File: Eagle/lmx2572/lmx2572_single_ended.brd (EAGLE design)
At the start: 38.1 x 36.9 mm, 36 parts

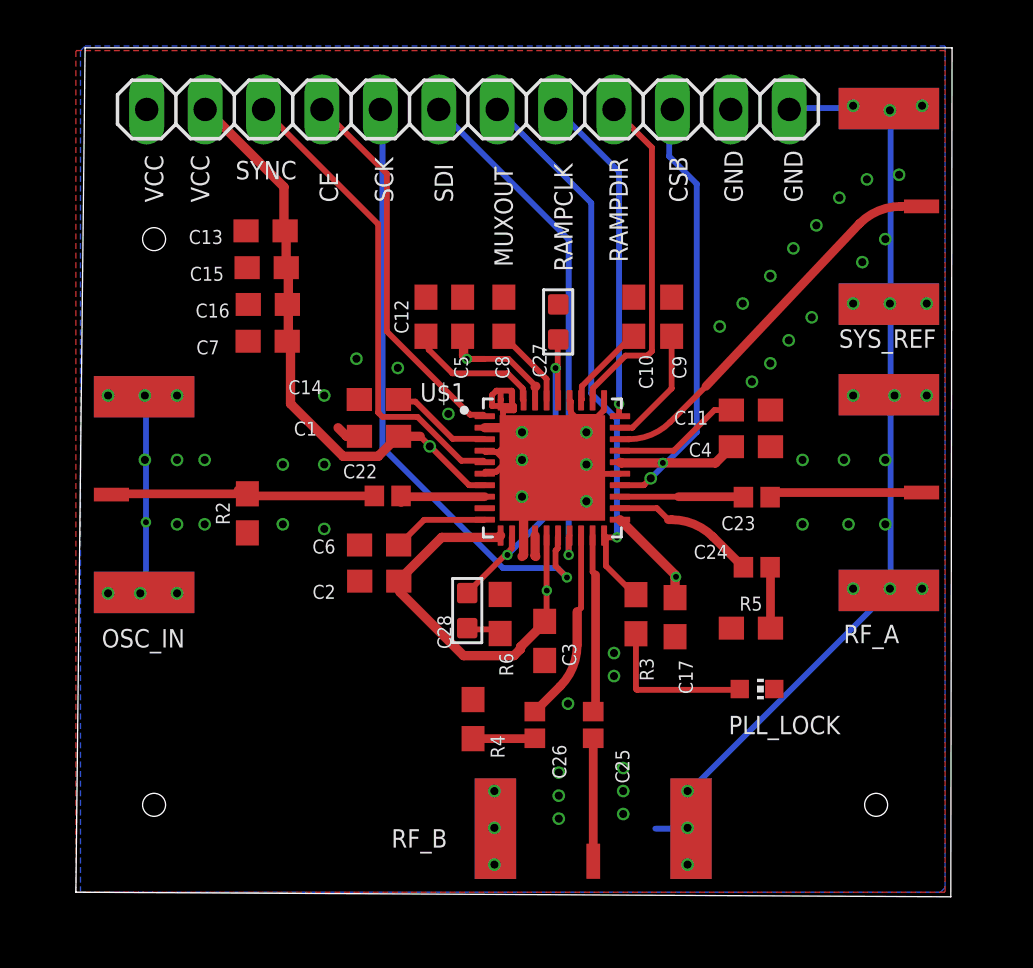
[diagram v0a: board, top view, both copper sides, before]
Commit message: added TCXO
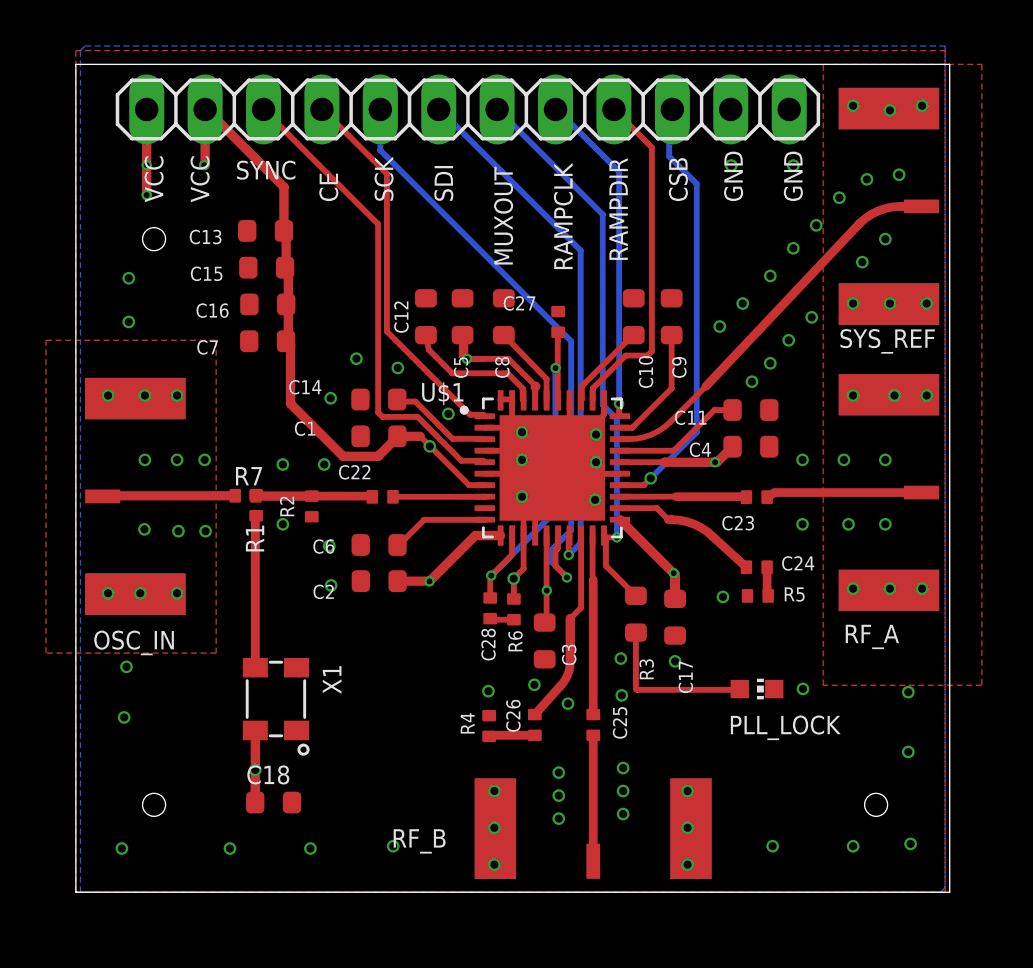
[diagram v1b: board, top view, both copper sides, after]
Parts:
- added C18: 10uF, oresat-rcl:.0603-B-NOSILK
- added R1, R7: 0, oresat-rcl:.0402-C-NOSILK
- added X1: ECS-TXO-3225, X-ECS-TXO-TCXO:3.2X2.5
- C1, C10, C11, C12, C13, C14, C15, C16, C17, C2, C3, C4, C5, C6, C7, C8, C9: device SparkFun-Capacitors:0603 -> oresat-rcl:.0603-B-NOSILK
- C22, C23, C24, C25, C26: device SparkFun-Capacitors:0402 -> oresat-rcl:.0402-C-NOSILK
- C27, C28: device OPL_Capacitor:C0603 -> oresat-rcl:.0402-C-NOSILK
- R2, R4, R5, R6: device SparkFun-Resistors:0603 -> oresat-rcl:.0402-C-NOSILK
- R3: device SparkFun-Resistors:0603 -> oresat-rcl:.0603-B-NOSILK
- moved R2 2.82 mm to (10.3, 16.8)
- moved R5 1.43 mm to (29.7, 12.9)
- moved C28 1.00 mm to (18.0, 12.3), turned to 90 degrees
- moved R4 0.76 mm to (18.0, 7.23)
- moved R6 0.63 mm to (19.1, 12.3)
- moved OSC_IN 0.39 mm to (0.02, 17.2)
- moved C22 0.22 mm to (13.3, 17.2)
- turned C27 to 270 degrees
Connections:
- new net N$11: OSC_IN.RF1, R7.2
- new net N$21: C22.1, R1.2, R2.2, R7.1
- net GND: now also C18.2, X1.2
- net N$9: now also R1.1, X1.3; no longer C22.1, OSC_IN.RF1, R2.2
- net VCC: now also C18.1, X1.4
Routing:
- net GND: track 75.9 -> 33.2 mm, vias 73 -> 95
- net N$11: track 0.00 -> 5.78 mm
- net N$9: track 12.1 -> 6.62 mm
- net N$21: track 0.00 -> 5.08 mm
- net VCC: track 58.2 -> 60.9 mm, vias 5 -> 10
- net N$23: track 2.70 -> 1.27 mm
- net N$24: track 15.1 -> 16.3 mm
- net N$22: track 2.73 -> 2.01 mm
- net SCK: track 27.2 -> 26.6 mm
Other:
- board size 38.1 x 36.9 mm -> 38 x 36 mm

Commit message: more vias
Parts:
- moved RF_A 0.20 mm to (38.0, 17.2)
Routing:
- net GND: track 33.2 -> 34.0 mm, vias 95 -> 97
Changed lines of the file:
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@@
 <drawing>
 <settings>
-<setting alwaysvectorfont="no"/>
+<setting alwaysvectorfont="yes"/>
 <setting verticaltext="up"/>
 </settings>
@@
 <layer number="14" name="Route14" color="22" fill="1" visible="no" active="no"/>
 <layer number="15" name="Route15" color="23" fill="1" visible="no" active="yes"/>
-<layer number="16" name="Bottom" color="1" fill="1" visible="no" active="yes"/>
+<layer number="16" name="Bottom" color="1" fill="1" visible="yes" active="yes"/>
 <layer number="17" name="Pads" color="2" fill="1" visible="yes" active="yes"/>
 <layer number="18" name="Vias" color="2" fill="1" visible="yes" active="yes"/>
@@
 <wire x1="22.6" y1="13.8" x2="22.6" y2="8.4" width="1.27" layer="29"/>
 <wire x1="22.6" y1="6.2" x2="22.6" y2="1" width="1.27" layer="29"/>
-<wire x1="30.6" y1="17.4" x2="37.4" y2="17.4" width="1.27" layer="29"/>
+<wire x1="30.7" y1="17.2" x2="37.5" y2="17.2" width="1.27" layer="29"/>
 <wire x1="27.4" y1="22.2" x2="35" y2="29.8" width="1.27" layer="29"/>
 <wire x1="35" y1="29.8" x2="37.2" y2="29.8" width="1.27" layer="29"/>
@@
 <attribute name="NAME" x="26.546" y="22.826" size="0.6096" layer="25" font="vector" ratio="20" rot="R90" align="bottom-center"/>
 </element>
-<element name="RF_A" library="J-Cinch-142-0701-851-SMA-end-launch" package="142-0701-851" value="142-0701-851" x="37.922" y="17.38" smashed="yes" rot="R270">
-<attribute name="NAME" x="33.382" y="10.83" size="0.8" layer="25" font="vector"/>
+<element name="RF_A" library="J-Cinch-142-0701-851-SMA-end-launch" package="142-0701-851" value="142-0701-851" x="37.962" y="17.18" smashed="yes" rot="R270">
+<attribute name="NAME" x="33.422" y="10.63" size="0.8" layer="25" font="vector"/>
 </element>
 <element name="RF_B" library="J-Cinch-142-0701-851-SMA-end-launch" package="142-0701-851" value="142-0701-851" x="22.498" y="0.2" smashed="yes" rot="R180">
@@
 </polygon>
 <polygon width="0.38" layer="1">
-<vertex x="0.4" y="36.6"/>
-<vertex x="37.8" y="36.6"/>
-<vertex x="37.8" y="0"/>
-<vertex x="0" y="0"/>
 <vertex x="0" y="36.6"/>
+<vertex x="39.62" y="36.6"/>
+<vertex x="39.62" y="-0.02"/>
+<vertex x="0" y="-0.02"/>
 </polygon>
 <wire x1="18.288" y1="2.76225" x2="18.2435" y2="2.766" width="0.254" layer="16"/>
-<wire x1="35.433" y1="13.1445" x2="35.356" y2="13.1255" width="0.254" layer="16"/>
-<wire x1="35.433" y1="21.62175" x2="35.356" y2="21.6345" width="0.254" layer="16"/>
+<wire x1="35.473" y1="12.9445" x2="35.396" y2="12.9255" width="0.254" layer="16"/>
+<wire x1="35.473" y1="21.42175" x2="35.396" y2="21.4345" width="0.254" layer="16"/>
 <wire x1="35.433" y1="25.527" x2="35.356" y2="25.5715" width="0.254" layer="16"/>
-<wire x1="35.433" y1="21.717" x2="35.356" y2="21.6345" width="0.254" layer="16"/>
+<wire x1="35.473" y1="21.517" x2="35.396" y2="21.4345" width="0.254" layer="16"/>
 <wire x1="26.76525" y1="4.47675" x2="26.76525" y2="2.8575" width="0.254" layer="16"/>
 <wire x1="26.76525" y1="2.8575" x2="26.7525" y2="2.766" width="0.254" layer="16"/>
-<wire x1="35.33775" y1="13.04925" x2="35.356" y2="13.1255" width="0.254" layer="16"/>
+<wire x1="35.37775" y1="12.84925" x2="35.396" y2="12.9255" width="0.254" layer="16"/>
 <wire x1="18.57375" y1="18.57375" x2="18.57375" y2="18.8595" width="0.254" layer="1"/>
 <wire x1="18.97" y1="20.17775" x2="18.8448" y2="20.30295" width="0.254" layer="1"/>
-<wire x1="18.57375" y1="20.574" x2="18.8448" y2="20.30295" width="0.254" layer="1"/>
 <wire x1="35.33775" y1="34.0995" x2="35.356" y2="34.0805" width="0.254" layer="16"/>
 <wire x1="31.0515" y1="34.0995" x2="31.02" y2="34.04" width="0.254" layer="16"/>
@@
 </polygon>
 <wire x1="19.729075" y1="16.670925" x2="19.579075" y2="16.520925" width="0.4064" layer="1"/>
-<via x="31.6" y="18.8" extent="1-16" drill="0.35"/>
-<via x="33.4" y="18.8" extent="1-16" drill="0.35"/>
-<via x="35.2" y="18.8" extent="1-16" drill="0.35"/>
-<via x="33.8" y="21.6" extent="1-16" drill="0.35"/>
-<via x="35.6" y="21.6" extent="1-16" drill="0.35"/>
-<via x="37" y="21.6" extent="1-16" drill="0.35"/>
-<via x="35.2" y="16" extent="1-16" drill="0.35"/>
-<via x="33.6" y="16" extent="1-16" drill="0.35"/>
-<via x="31.6" y="16" extent="1-16" drill="0.35"/>
-<via x="33.8" y="13.2" extent="1-16" drill="0.35"/>
-<via x="35.4" y="13.2" extent="1-16" drill="0.35"/>
-<via x="36.8" y="13.2" extent="1-16" drill="0.35"/>
+<via x="31.52" y="18.82" extent="1-16" drill="0.35"/>
+<via x="33.42" y="18.62" extent="1-16" drill="0.35"/>
+<via x="35.2" y="18.62" extent="1-16" drill="0.35"/>
+<via x="33.78" y="21.42" extent="1-16" drill="0.35"/>
+<via x="35.58" y="21.44" extent="1-16" drill="0.35"/>
+<via x="37" y="21.46" extent="1-16" drill="0.35"/>
+<via x="35.26" y="15.88" extent="1-16" drill="0.35"/>
+<via x="33.58" y="15.8" extent="1-16" drill="0.35"/>
+<via x="31.54" y="15.78" extent="1-16" drill="0.35"/>
+<via x="33.86" y="13" extent="1-16" drill="0.35"/>
+<via x="35.46" y="13" extent="1-16" drill="0.35"/>
+<via x="36.82" y="12.96" extent="1-16" drill="0.35"/>
 <via x="37" y="25.6" extent="1-16" drill="0.35"/>
 <via x="35.4" y="25.6" extent="1-16" drill="0.35"/>
@@
 <via x="22.62" y="18.7" extent="1-16" drill="0.35"/>
 <via x="22.58" y="17.06" extent="1-16" drill="0.35"/>
+<wire x1="18.47" y1="21.39" x2="18.47" y2="20.925175" width="0.254" layer="1"/>
+<wire x1="18.47" y1="20.925175" x2="18.479" y2="20.916175" width="0.254" layer="1"/>
+<wire x1="18.479" y1="20.916175" x2="18.479" y2="20.66875" width="0.254" layer="1"/>
+<wire x1="18.479" y1="20.66875" x2="18.8448" y2="20.30295" width="0.254" layer="1"/>
+<via x="15.1" y="27.2" extent="1-16" drill="0.35"/>
+<via x="16.86" y="27.28" extent="1-16" drill="0.35"/>
+<polygon width="0.254" layer="1" thermals="no">
+<vertex x="16.52" y="5.7"/>
+<vertex x="16.52" y="-1.3"/>
+<vertex x="28.96" y="-1.3"/>
+<vertex x="28.96" y="5.7"/>
+</polygon>
 <wire x1="19" y1="19.3" x2="18.57375" y2="18.8595" width="0" layer="19" extent="1-1"/>
 <wire x1="19.14525" y1="19.90725" x2="19" y2="19.3" width="0" layer="19" extent="1-1"/>
 <wire x1="19.2" y1="18.2" x2="19.4" y2="18.8" width="0" layer="19" extent="1-1"/>
-<wire x1="22.97" y1="21.39" x2="22.62" y2="19.9" width="0" layer="19" extent="1-1"/>
 </signal>
 <signal name="N$1">
@@
 <contactref element="C23" pad="2"/>
 <contactref element="RF_A" pad="RF1"/>
-<wire x1="30.06" y1="17.18" x2="30.39" y2="17.38" width="0.381" layer="1"/>
-<wire x1="30.39" y1="17.38" x2="36.776" y2="17.38" width="0.38" layer="1"/>
+<wire x1="36.816" y1="17.18" x2="30.06" y2="17.18" width="0.38" layer="1"/>
 </signal>
 <signal name="N$18" class="2">
@@
 <wire x1="20.955" y1="24.003" x2="20.974" y2="24.35" width="0.254" layer="1"/>
 <wire x1="20.955" y1="21.43125" x2="20.97" y2="21.39" width="0.254" layer="1"/>
-<wire x1="20.85975" y1="16.564" x2="20.85975" y2="22.79325" width="0.254" layer="16"/>
-<wire x1="18.06425" y1="13.7685" x2="20.85975" y2="16.564" width="0.254" layer="16"/>
-<wire x1="20.85975" y1="22.79325" x2="20.955" y2="22.79325" width="0.254" layer="1"/>
-<via x="20.85975" y="22.79325" extent="1-16" drill="0.254"/>
+<wire x1="20.95975" y1="16.664" x2="20.95975" y2="22.79325" width="0.254" layer="16"/>
+<wire x1="18.06425" y1="13.7685" x2="20.95975" y2="16.664" width="0.254" layer="16"/>
+<wire x1="20.95975" y1="22.79325" x2="20.955" y2="22.79325" width="0.254" layer="1"/>
+<via x="20.95975" y="22.79325" extent="1-16" drill="0.254"/>
 <via x="18.06425" y="13.7685" extent="1-16" drill="0.254"/>
 <wire x1="18.018" y1="12.796" x2="18.018" y2="13.72225" width="0.254" layer="1"/>
@@
 <wire x1="21.355" y1="13.6875" x2="20.85975" y2="14.18275" width="0.254" layer="1"/>
 <wire x1="20.955" y1="15.4305" x2="20.97" y2="15.51" width="0.254" layer="1"/>
-<wire x1="13.24" y1="34.04" x2="13.335" y2="34.00425" width="0.254" layer="16"/>
 <via x="21.355" y="13.6875" extent="1-16" drill="0.254"/>
 <wire x1="13.24" y1="34.04" x2="13.24" y2="32.26" width="0.254" layer="16"/>
